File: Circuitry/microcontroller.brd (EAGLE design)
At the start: 30.5 x 50.5 mm, 16 parts

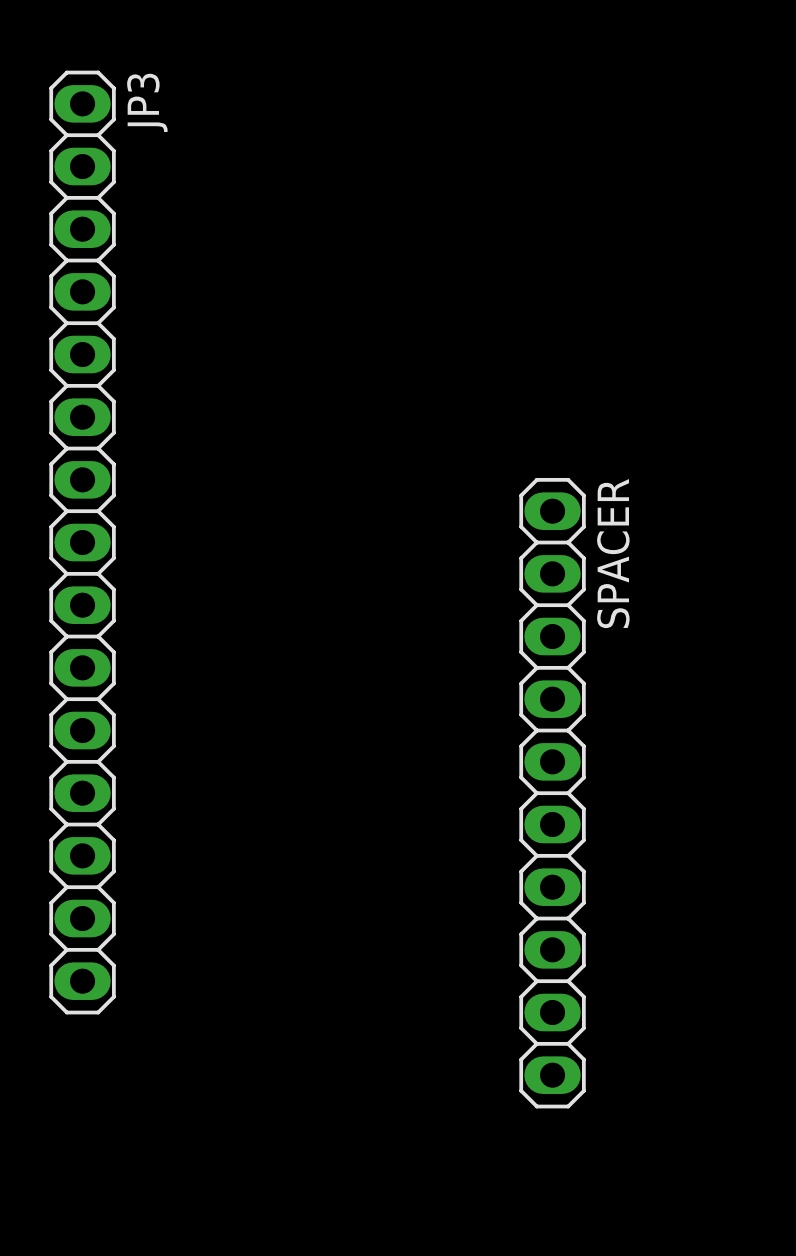
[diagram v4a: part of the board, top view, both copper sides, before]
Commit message: remove header pins
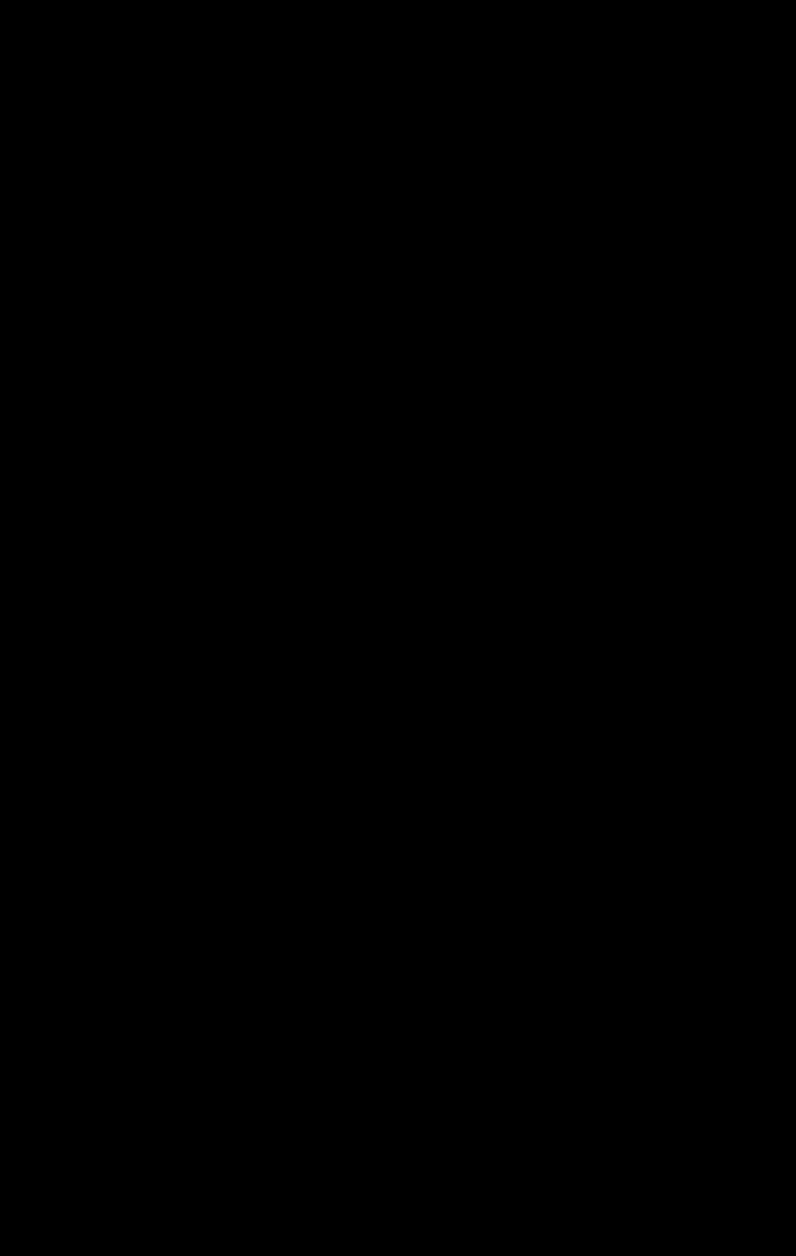
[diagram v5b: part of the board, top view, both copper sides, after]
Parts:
- removed JP3: (no value), pinhead:1X15
- removed SPACER: (no value), pinhead:1X10
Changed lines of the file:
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@@
 <attribute name="VALUE" x="28.575" y="41.91" size="1.27" layer="28" ratio="10" rot="MR180"/>
-</element>
-<element name="JP3" library="pinhead" library_urn="urn:adsk.eagle:library:325" package="1X15" package3d_urn="urn:adsk.eagle:package:22424/2" value="" x="-24.13" y="35.56" smashed="yes" rot="R270">
-<attribute name="NAME" x="-22.3012" y="54.6862" size="1.27" layer="25" ratio="10" rot="R270"/>
-<attribute name="POPULARITY" value="4" x="-24.13" y="35.56" size="1.778" layer="27" rot="R270" display="off"/>
-<attribute name="VALUE" x="-27.305" y="54.61" size="1.27" layer="27" rot="R270"/>
 </element>
 <element name="JP4" library="pinhead" library_urn="urn:adsk.eagle:library:325" package="1X15" package3d_urn="urn:adsk.eagle:package:22424/2" value="" x="11.43" y="33.02" smashed="yes" rot="R270">
@@
 <attribute name="VALUE" x="8.255" y="52.07" size="1.27" layer="27" rot="R270"/>
 </element>
-<element name="SPACER" library="pinhead" library_urn="urn:adsk.eagle:library:325" package="1X10" package3d_urn="urn:adsk.eagle:package:22406/2" value="" x="-5.08" y="25.4" smashed="yes" rot="R270">
-<attribute name="NAME" x="-3.2512" y="38.1762" size="1.27" layer="25" ratio="10" rot="R270"/>
-<attribute name="POPULARITY" value="35" x="-5.08" y="25.4" size="1.778" layer="27" rot="R270" display="off"/>
-<attribute name="VALUE" x="-8.255" y="38.1" size="1.27" layer="27" rot="R270"/>
-</element>
 <element name="JP1" library="pinhead" library_urn="urn:adsk.eagle:library:325" package="1X02" package3d_urn="urn:adsk.eagle:package:22435/2" value="" x="34.29" y="16.51" smashed="yes" rot="R270">
